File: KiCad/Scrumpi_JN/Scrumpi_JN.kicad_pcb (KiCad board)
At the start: 4 copper layers, 165.1 x 127 mm, 203 parts

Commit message: Updated Silk Screen.
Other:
- board text added: "+5V"
- board text added: "-7V"
- board text added: "<"
- board text added: "<LEDS>"
- board text added: ">"
- board text added: "GND"
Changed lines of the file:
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@@
 		(tenting front back)
 		(pcbplotparams
-			(layerselection 0x00000000_00000000_55555555_5755f501)
+			(layerselection 0x00000000_00000000_55555555_5755552c)
 			(plot_on_all_layers_selection 0x00000000_00000000_00000000_00000000)
 			(disableapertmacros no)
@@
 	)
 	(gr_line
-		(start 79.725 41.016721)
-		(end 79.555 83.82)
+		(start 79.68 99.98)
+		(end 79.755 129.7)
 		(stroke
 			(width 0.6)
@@
 	)
 	(gr_line
-		(start 79.925 99.846721)
-		(end 79.755 129.7)
+		(start 79.725 41.016721)
+		(end 79.555 83.82)
 		(stroke
 			(width 0.6)
@@
 		)
 	)
+	(gr_text "GND"
+		(at 108.77 135.77 0)
+		(layer "F.SilkS")
+		(effects
+			(font
+				(size 1.6 1.6)
+				(thickness 0.3)
+				(bold yes)
+			)
+			(justify left bottom)
+		)
+	)
+	(gr_text "+5V"
+		(at 114.66 135.67 0)
+		(layer "F.SilkS")
+		(effects
+			(font
+				(size 1.6 1.6)
+				(thickness 0.3)
+				(bold yes)
+			)
+			(justify left bottom)
+		)
+	)
+	(gr_text "-7V"
+		(at 121.2 135.6 0)
+		(layer "F.SilkS")
+		(effects
+			(font
+				(size 1.6 1.6)
+				(thickness 0.3)
+				(bold yes)
+			)
+			(justify left bottom)
+		)
+	)
 	(gr_text "PCB-J1"
 		(at 113.51 150.82 0)
@@
 		)
 	)
-	(gr_text "SCRUMPI"
-		(at 76.08 151.24 0)
+	(gr_text "<LEDS>"
+		(at 80.87 99.66 90)
 		(layer "F.SilkS")
 		(effects
 			(font
-				(size 6 5.4)
-				(thickness 0.6)
+				(size 2.5 2.5)
+				(thickness 0.4)
 			)
 			(justify left bottom)
 		)
 	)
-	(gr_text "PCB-J1"
-		(at 207.55 27.75 180)
-		(layer "B.SilkS")
+	(gr_text ">"
+		(at 80.96 43 90)
+		(layer "F.SilkS")
 		(effects
 			(font
 				(size 2.5 2.5)
-				(thickness 0.5)
-				(bold yes)
+				(thickness 0.4)
+			)
+			(justify left bottom)
+		)
+	)
+	(gr_text "<"
+		(at 81.03 131.4 90)
+		(layer "F.SilkS")
+		(effects
+			(font
+				(size 2.5 2.5)
+				(thickness 0.4)
 			)
 			(justify left bottom)
@@
 	)
 	(gr_text "SCRUMPI"
-		(at 241.75 27.55 180)
-		(layer "B.SilkS")
+		(at 76.08 151.24 0)
+		(layer "F.SilkS")
 		(effects
 			(font
-				(size 5.3 5)
-				(thickness 0.8)
+				(size 6 5.4)
+				(thickness 0.6)
 			)
 			(justify left bottom)

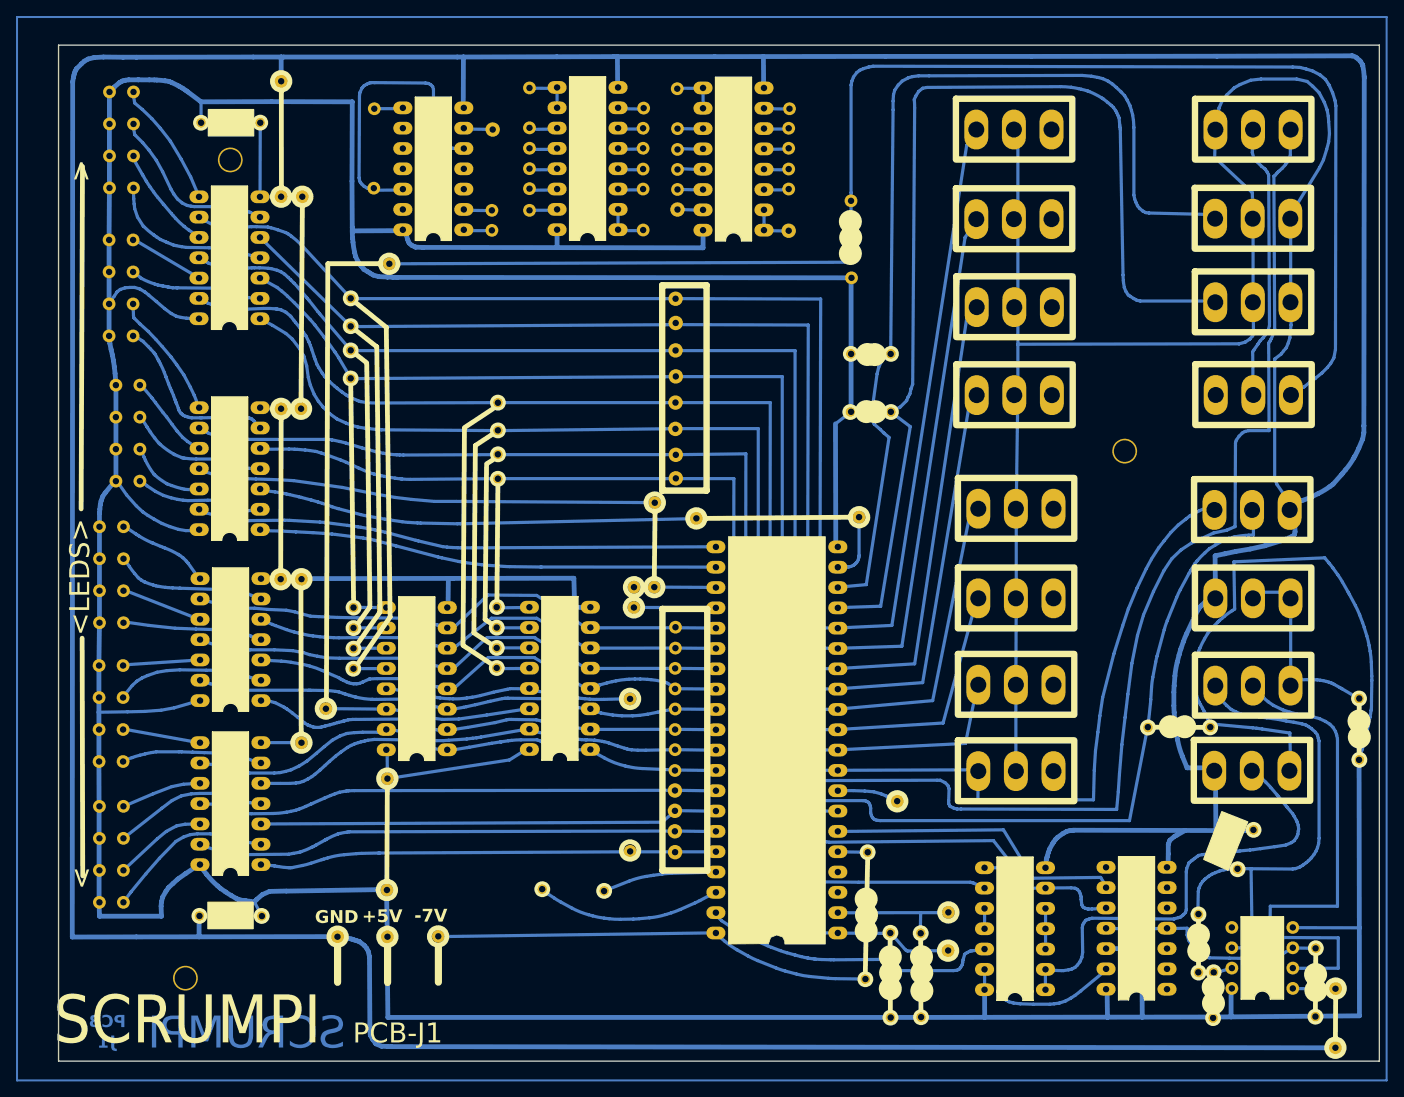
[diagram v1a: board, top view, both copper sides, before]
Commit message: Updated Silk Screen.
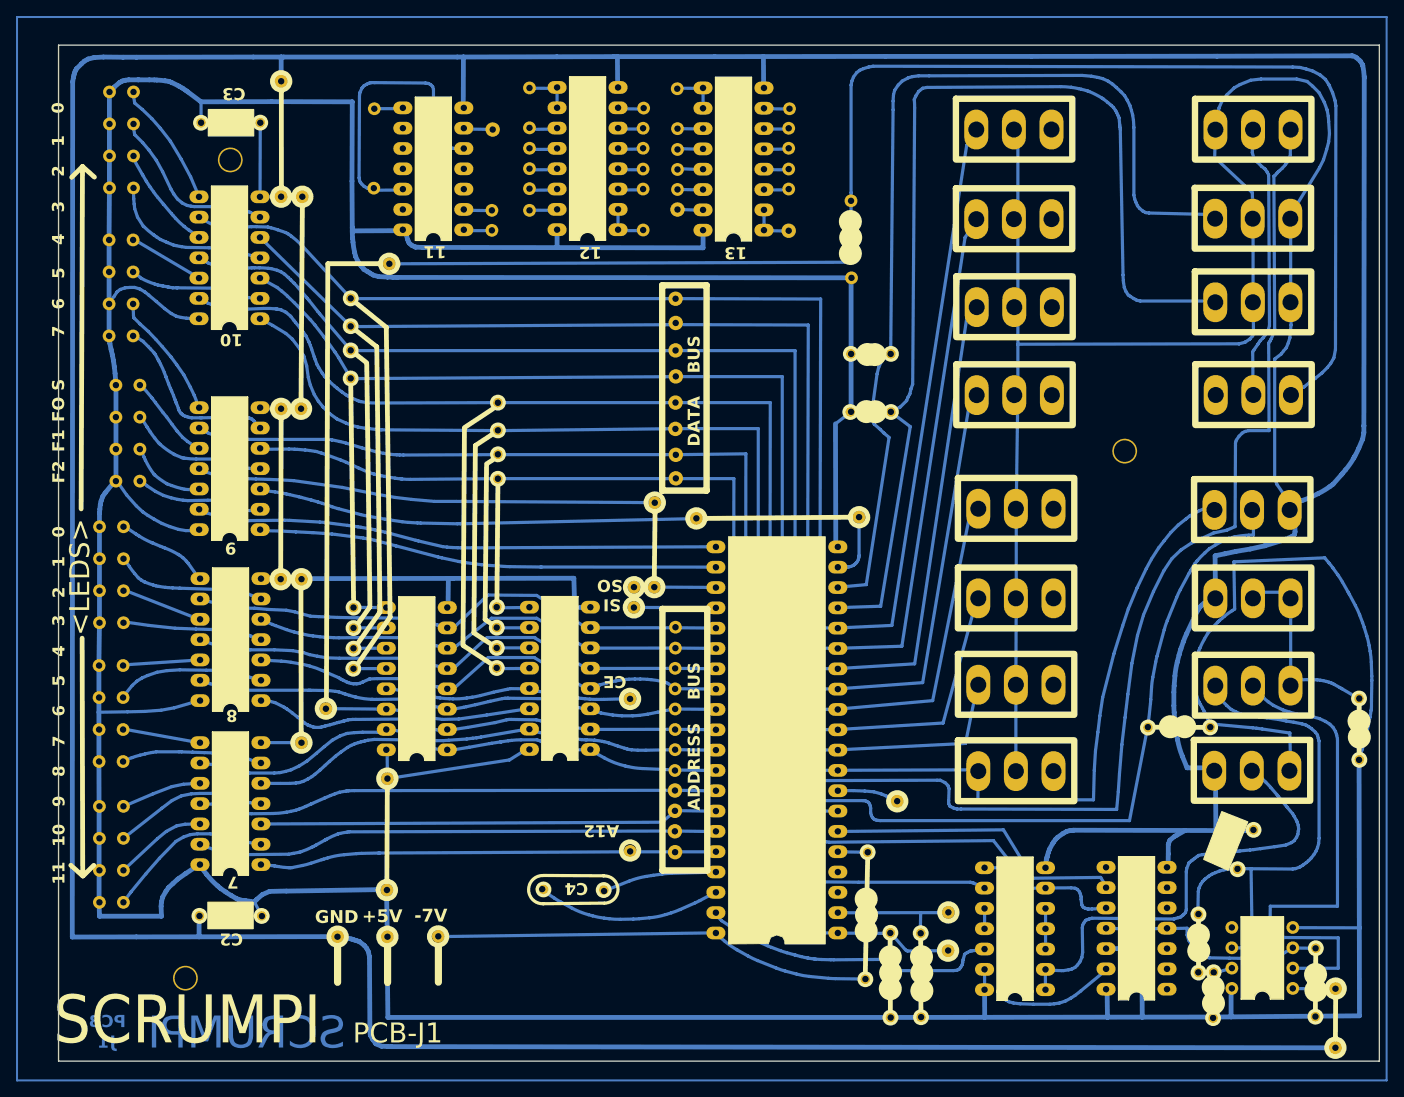
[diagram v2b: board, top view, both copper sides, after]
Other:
- board text added: "0"
- board text added: "1"
- board text added: "10"
- board text added: "11"
- board text added: "12"
- board text added: "13"
- board text added: "2"
- board text added: "3"
- board text added: "4"
- board text added: "5"
- board text added: "6"
- board text added: "7"
- board text added: "8"
- board text added: "9"
- board text added: "A12"
- board text added: "ADDRESS BUS"
- board text added: "C2"
- board text added: "C3"
- board text added: "C4"
- board text added: "CE"
- board text added: "DATA BUS"
- board text added: "F1"
- board text added: "F2"
- board text added: "FO"
- board text added: "S"
- board text added: "SI"
- board text added: "SO"
- board text removed: "<"
- board text removed: ">"

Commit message: Updated Silk Screen.
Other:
- board text added: "D0"
- board text added: "D1"
- board text added: "D2"
- board text added: "D3"
- board text added: "D4"
- board text added: "D5"
- board text added: "D6"
- board text added: "D7"
- board text added: "R10"
- board text added: "R2"
- board text added: "R9"
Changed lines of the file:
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@@
 	)
 	(gr_rect
-		(start 71.54 22.335)
-		(end 242.74 155.26)
-		(stroke
-			(width 0.254)
-			(type default)
-		)
-		(fill no)
-		(layer "B.Cu")
-	)
-	(gr_rect
 		(start 75.85 25.7)
 		(end 242.725 154.225)
@@
 	)
 	(gr_line
-		(start 78.26 128.366721)
-		(end 79.755 129.7)
+		(start 78.855 128.356721)
+		(end 80.35 129.69)
 		(stroke
 			(width 0.6)
@@
 	)
 	(gr_line
-		(start 78.37 42.38)
-		(end 79.725 41.016721)
+		(start 78.965 42.37)
+		(end 80.32 41.006721)
 		(stroke
 			(width 0.6)
@@
 	)
 	(gr_line
-		(start 79.68 99.98)
-		(end 79.755 129.7)
+		(start 80.275 99.97)
+		(end 80.35 129.69)
 		(stroke
 			(width 0.6)
@@
 	)
 	(gr_line
-		(start 79.725 41.016721)
-		(end 79.555 83.82)
+		(start 80.32 41.006721)
+		(end 80.15 83.81)
 		(stroke
 			(width 0.6)
@@
 	)
 	(gr_line
-		(start 79.725 41.016721)
-		(end 81.22 42.35)
+		(start 80.32 41.006721)
+		(end 81.815 42.34)
 		(stroke
 			(width 0.6)
@@
 	)
 	(gr_line
-		(start 81.14 128.37336)
-		(end 79.7975 129.706639)
+		(start 81.735 128.36336)
+		(end 80.3925 129.696639)
 		(stroke
 			(width 0.6)
@@
 		(layer "B.SilkS")
 	)
-	(gr_line
-		(start 88.95 44)
-		(end 94.6 44)
-		(stroke
-			(width 0.1)
-			(type default)
-		)
-		(layer "Dwgs.User")
-	)
 	(gr_rect
-		(start 76.73 25.85)
-		(end 241.83 152.85)
+		(start 76.54 26.3)
+		(end 241.64 153.3)
 		(stroke
 			(width 0.0381)
@@
 		)
 		(fill no)
+		(locked yes)
 		(layer "Edge.Cuts")
 	)
@@
 	)
 	(gr_text "0"
-		(at 77.55 34.41 90)
+		(at 78.29 34.34 90)
 		(layer "F.SilkS")
 		(effects
@@
 	)
 	(gr_text "1"
-		(at 77.58 38.54 90)
+		(at 78.32 38.47 90)
 		(layer "F.SilkS")
 		(effects
@@
 	)
 	(gr_text "2"
-		(at 77.59 42.31 90)
+		(at 78.33 42.24 90)
 		(layer "F.SilkS")
 		(effects
@@
 	)
 	(gr_text "3"
-		(at 77.59 46.76 90)
+		(at 78.33 46.69 90)
 		(layer "F.SilkS")
 		(effects
@@
 	)
 	(gr_text "4"
-		(at 77.6 50.83 90)
+		(at 78.34 50.76 90)
 		(layer "F.SilkS")
 		(effects
@@
 	)
 	(gr_text "6"
-		(at 77.6 58.89 90)
+		(at 78.34 58.82 90)
 		(layer "F.SilkS")
 		(effects
@@
 	)
 	(gr_text "S"
-		(at 77.6 69.05 90)
+		(at 78.34 68.98 90)
 		(layer "F.SilkS")
 		(effects
@@
 	)
 	(gr_text "7"
-		(at 77.61 62.34 90)
+		(at 78.35 62.27 90)
 		(layer "F.SilkS")
 		(effects
@@
 	)
 	(gr_text "FO"
-		(at 77.61 72.95 90)
+		(at 78.35 72.88 90)
 		(layer "F.SilkS")
 		(effects
@@
 	)
 	(gr_text "5"
-		(at 77.62 55.05 90)
+		(at 78.36 54.98 90)
 		(layer "F.SilkS")
 		(effects
@@
 	)
 	(gr_text "F1"
-		(at 77.62 76.71 90)
+		(at 78.36 76.64 90)
 		(layer "F.SilkS")
 		(effects
@@
 	)
 	(gr_text "F2"
-		(at 77.63 80.62 90)
+		(at 78.37 80.55 90)
 		(layer "F.SilkS")
 		(effects
@@
 	)
 	(gr_text "0"
-		(at 77.63 87.41 90)
+		(at 78.37 87.34 90)
 		(layer "F.SilkS")
 		(effects
@@
 	)
 	(gr_text "3"
-		(at 77.63 98.48 90)
+		(at 78.37 98.41 90)
 		(layer "F.SilkS")
 		(effects
@@
 	)
 	(gr_text "1"
-		(at 77.64 91.15 90)
+		(at 78.38 91.08 90)
 		(layer "F.SilkS")
 		(effects
@@
 	)
 	(gr_text "2"
-		(at 77.65 94.97 90)
+		(at 78.39 94.9 90)
 		(layer "F.SilkS")
 		(effects
@@
 	)
 	(gr_text "4"
-		(at 77.65 102.31 90)
+		(at 78.39 102.24 90)
 		(layer "F.SilkS")
 		(effects
@@
 	)
 	(gr_text "5"
-		(at 77.65 106 90)
+		(at 78.39 105.93 90)
 		(layer "F.SilkS")
 		(effects
@@
 	)
 	(gr_text "6"
-		(at 77.65 109.77 90)
+		(at 78.39 109.7 90)
 		(layer "F.SilkS")
 		(effects
@@
 	)
 	(gr_text "11"
-		(at 77.65 130.77 90)
+		(at 78.39 130.7 90)
 		(layer "F.SilkS")
 		(effects
@@
 	)
 	(gr_text "7"
-		(at 77.66 113.58 90)
+		(at 78.4 113.51 90)
 		(layer "F.SilkS")
 		(effects
@@
 	)
 	(gr_text "8"
-		(at 77.66 117.32 90)
+		(at 78.4 117.25 90)
 		(layer "F.SilkS")
 		(effects
@@
 	)
 	(gr_text "9"
-		(at 77.66 121.08 90)
+		(at 78.4 121.01 90)
 		(layer "F.SilkS")
 		(effects
@@
 	)
 	(gr_text "10"
-		(at 77.66 126.05 90)
+		(at 78.4 125.98 90)
 		(layer "F.SilkS")
 		(effects
@@
 		)
 	)
+	(gr_text "R2"
+		(at 173.36 51.3 90)
+		(layer "F.SilkS")
+		(effects
+			(font
+				(size 1.5 1.5)
+				(thickness 0.3)
+				(bold yes)
+			)
+			(justify left bottom)
+		)
+	)
+	(gr_text "D0"
+		(at 206.21 38.05 90)
+		(layer "F.SilkS")
+		(effects
+			(font
+				(size 1.5 1.5)
+				(thickness 0.3)
+				(bold yes)
+			)
+			(justify left bottom)
+		)
+	)
+	(gr_text "D1"
+		(at 206.24 48.97 90)
+		(layer "F.SilkS")
+		(effects
+			(font
+				(size 1.5 1.5)
+				(thickness 0.3)
+				(bold yes)
+			)
+			(justify left bottom)
+		)
+	)
+	(gr_text "D2"
+		(at 206.26 59.79 90)
+		(layer "F.SilkS")
+		(effects
+			(font
+				(size 1.5 1.5)
+				(thickness 0.3)
+				(bold yes)
+			)
+			(justify left bottom)
+		)
+	)
+	(gr_text "D3"
+		(at 206.28 70.75 90)
+		(layer "F.SilkS")
+		(effects
+			(font
+				(size 1.5 1.5)
+				(thickness 0.3)
+				(bold yes)
+			)
+			(justify left bottom)
+		)
+	)
+	(gr_text "D4"
+		(at 206.31 85.14 90)
+		(layer "F.SilkS")
+		(effects
+			(font
+				(size 1.5 1.5)
+				(thickness 0.3)
+				(bold yes)
+			)
+			(justify left bottom)
+		)
+	)
+	(gr_text "D5\n"
+		(at 206.36 96.44 90)
+		(layer "F.SilkS")
+		(effects
+			(font
+				(size 1.5 1.5)
+				(thickness 0.3)
+				(bold yes)
+			)
+			(justify left bottom)
+		)
+	)
+	(gr_text "D6"
+		(at 206.41 107.09 90)
+		(layer "F.SilkS")
+		(effects
+			(font
+				(size 1.5 1.5)
+				(thickness 0.3)
+				(bold yes)
+			)
+			(justify left bottom)
+		)
+	)
+	(gr_text "D7"
+		(at 206.45 117.84 90)
+		(layer "F.SilkS")
+		(effects
+			(font
+				(size 1.5 1.5)
+				(thickness 0.3)
+				(bold yes)
+			)
+			(justify left bottom)
+		)
+	)
 	(gr_text "9"
 		(at 98.95 87.86 180)
@@
 		)
 	)
+	(gr_text "R9"
+		(at 179.82 74.01 180)
+		(layer "F.SilkS")
+		(effects
+			(font
+				(size 1.5 1.5)
+				(thickness 0.3)
+				(bold yes)
+			)
+			(justify left bottom)
+		)
+	)
+	(gr_text "R10"
+		(at 180.67 66.69 180)
+		(layer "F.SilkS")
+		(effects
+			(font
+				(size 1.5 1.5)
+				(thickness 0.3)
+				(bold yes)
+			)
+			(justify left bottom)
+		)
+	)
 	(gr_text "GND"
 		(at 108.77 135.77 0)
@@
 	)
 	(gr_text "<LEDS>"
-		(at 80.87 99.66 90)
+		(at 81.465 99.65 90)
 		(layer "F.SilkS")
 		(effects

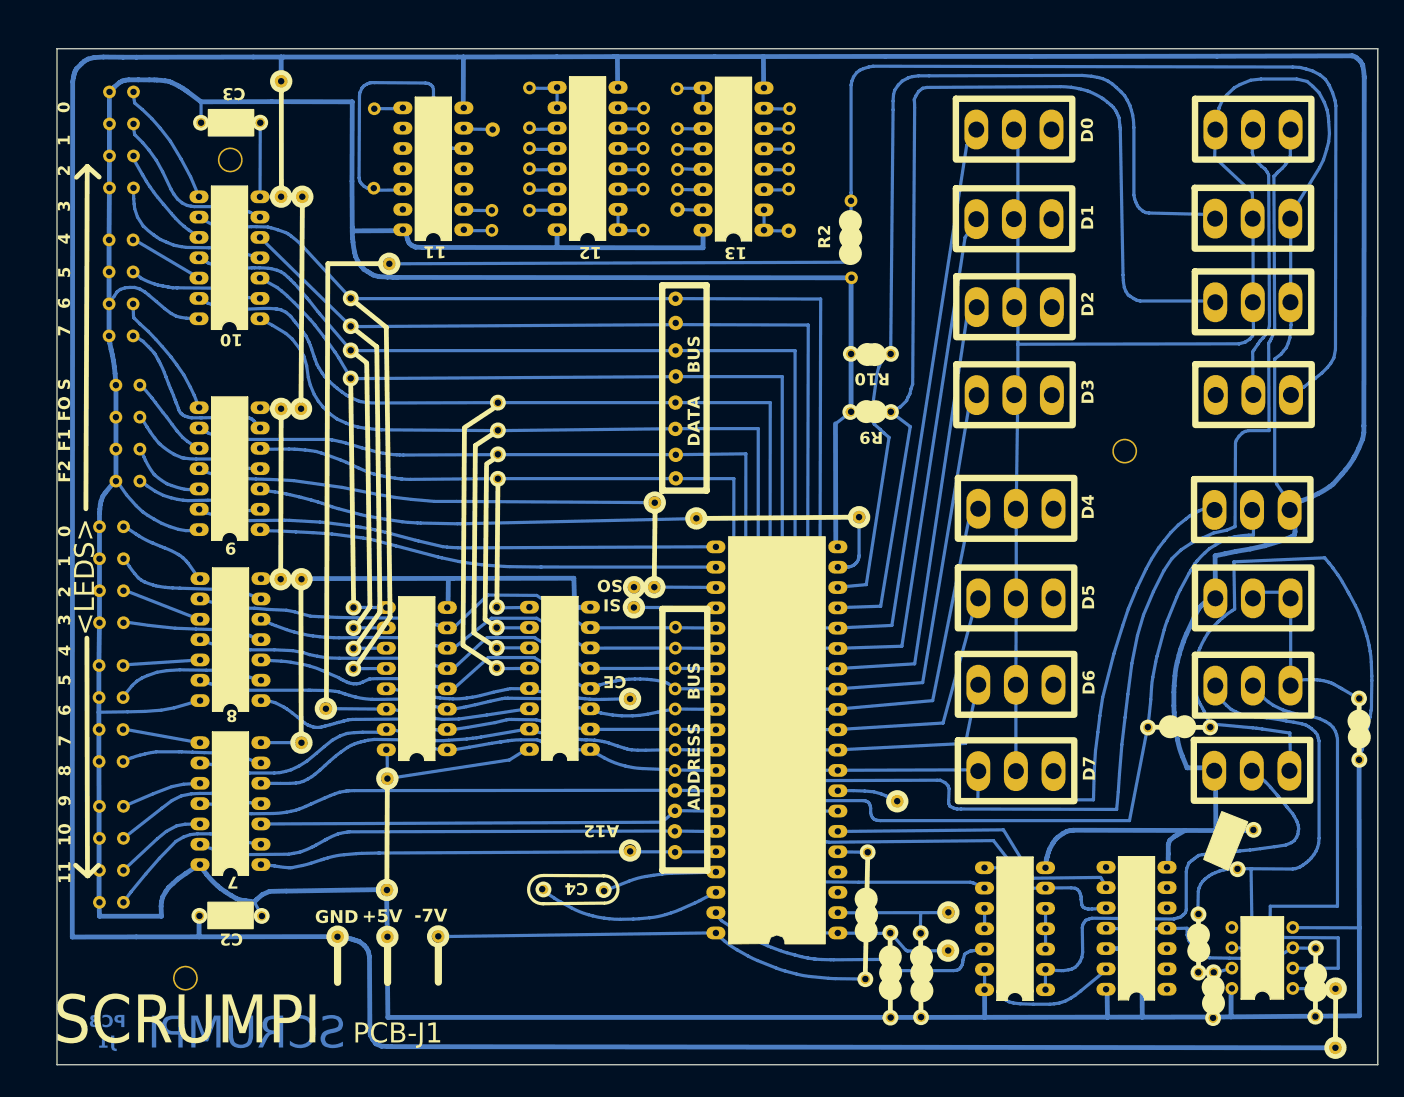
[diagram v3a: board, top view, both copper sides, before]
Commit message: Resized the board.
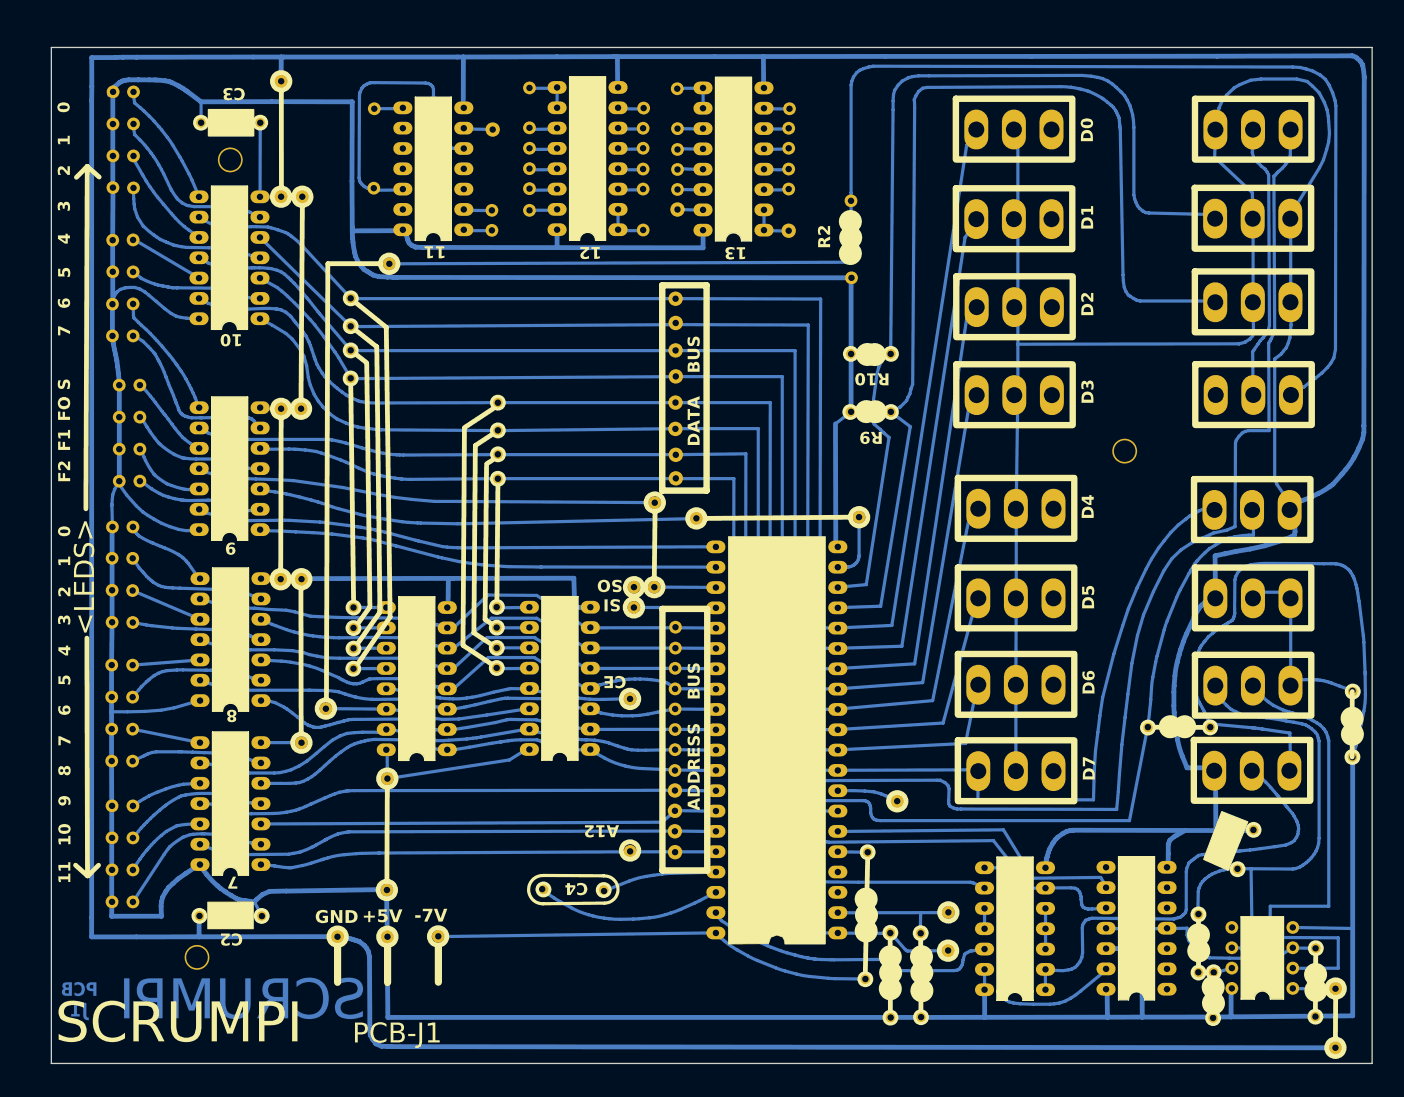
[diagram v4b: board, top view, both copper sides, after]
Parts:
- moved REF** 2.98 mm to (94.0, 139.9)
- moved ? 1.62 mm to (83.5, 86.1)
- moved ? 1.58 mm to (83.4, 94.0)
- moved ? 1.58 mm to (83.4, 98.0)
- moved ? 1.58 mm to (83.4, 90.0)
- moved ? 1.58 mm to (83.4, 107.3)
- moved ? 1.58 mm to (83.4, 132.9)
- moved ? 1.58 mm to (83.4, 120.9)
- moved ? 1.58 mm to (83.4, 124.9)
- moved ? 1.58 mm to (83.4, 128.9)
- moved ? 1.58 mm to (83.4, 103.3)
- moved ? 1.58 mm to (83.4, 115.3)
- moved ? 1.58 mm to (83.4, 111.3)
- moved ? 1.28 mm to (238.5, 106.6)
- moved ? 1.19 mm to (86.0, 107.3)
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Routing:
- net (no net): track 5836.7 -> 5807.5 mm
